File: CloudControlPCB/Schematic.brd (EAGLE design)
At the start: 62.2 x 61.9 mm, 29 parts, among them J1 AUDIO_JACK_TRRSSMD_RA, U1 LPC4088FBD208, U2 SGTL5000XNLA3R2, U3 LD1117S33CTR, X1 PHB_1MM27_2X05_SNT

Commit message: Fixed 1.8V regulator connections
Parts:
- moved U$1 1.27 mm to (15.2, 81.3)
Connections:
- net GND: no longer U$1.4

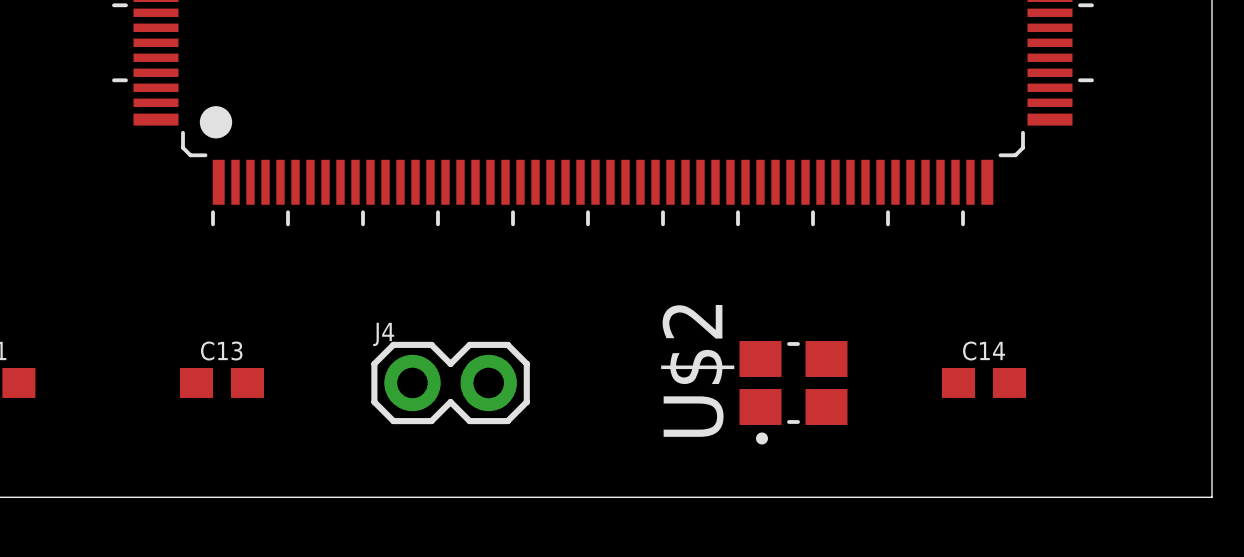
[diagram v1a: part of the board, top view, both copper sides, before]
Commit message: Connected Crystal on layout
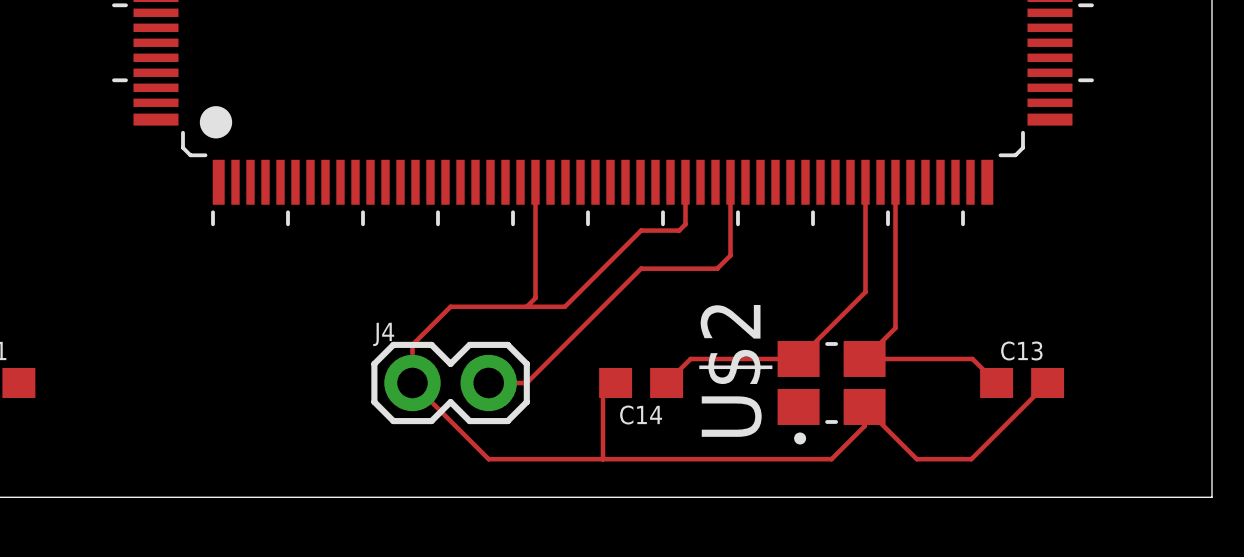
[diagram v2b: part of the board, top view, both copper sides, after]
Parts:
- moved C13 26.7 mm to (63.5, 38.1)
- moved C14 11.4 mm to (50.8, 38.1), turned to 180 degrees
- moved U$2 1.27 mm to (57.1, 38.1)
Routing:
- net GND: track 0.00 -> 45.5 mm
- net N$18: track 0.00 -> 12.3 mm
- net N$3: track 0.00 -> 11.5 mm
- net N$19: track 0.00 -> 11.0 mm
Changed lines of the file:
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@@
 <attribute name="VALUE" x="11.43" y="55.118" size="0.6096" layer="27" font="vector" ratio="20" align="top-center"/>
 </element>
-<element name="C13" library="SparkFun-Capacitors" package="0603" value="18pF" x="36.83" y="38.1">
-<attribute name="NAME" x="36.83" y="38.862" size="0.6096" layer="25" font="vector" ratio="20" align="bottom-center"/>
-<attribute name="PROD_ID" value="CAP-08267" x="113.03" y="-71.12" size="1.778" layer="27" display="off"/>
-<attribute name="VALUE" x="36.83" y="37.338" size="0.6096" layer="27" font="vector" ratio="20" align="top-center"/>
-</element>
-<element name="C14" library="SparkFun-Capacitors" package="0603" value="18pF" x="62.23" y="38.1">
-<attribute name="NAME" x="62.23" y="38.862" size="0.6096" layer="25" font="vector" ratio="20" align="bottom-center"/>
-<attribute name="PROD_ID" value="CAP-08267" x="142.24" y="-71.12" size="1.778" layer="27" display="off"/>
-<attribute name="VALUE" x="62.23" y="37.338" size="0.6096" layer="27" font="vector" ratio="20" align="top-center"/>
+<element name="C13" library="SparkFun-Capacitors" package="0603" value="18pF" x="63.5" y="38.1">
+<attribute name="NAME" x="63.5" y="38.862" size="0.6096" layer="25" font="vector" ratio="20" align="bottom-center"/>
+<attribute name="PROD_ID" value="CAP-08267" x="139.7" y="-71.12" size="1.778" layer="27" display="off"/>
+<attribute name="VALUE" x="63.5" y="37.338" size="0.6096" layer="27" font="vector" ratio="20" align="top-center"/>
+</element>
+<element name="C14" library="SparkFun-Capacitors" package="0603" value="18pF" x="50.8" y="38.1" rot="R180">
+<attribute name="NAME" x="50.8" y="37.338" size="0.6096" layer="25" font="vector" ratio="20" rot="R180" align="bottom-center"/>
+<attribute name="PROD_ID" value="CAP-08267" x="-29.21" y="147.32" size="1.778" layer="27" rot="R180" display="off"/>
+<attribute name="VALUE" x="50.8" y="38.862" size="0.6096" layer="27" font="vector" ratio="20" rot="R180" align="top-center"/>
 </element>
 <element name="C2" library="SparkFun-Capacitors" package="0603" value="0.1uF" x="19.05" y="48.26" rot="R180">
@@
 <attribute name="VALUE" x="27.178" y="69.85" size="0.6096" layer="27" font="vector" ratio="20" rot="R270" align="top-center"/>
 </element>
-<element name="U$2" library="XTAL_FA-238_25.0000MB-C3" package="XTAL_FA-238_25.0000MB-C3" value="XTAL_FA-238_25.0000MB-C3" x="55.88" y="38.1" rot="R90">
-<attribute name="VALUE" x="64.00721875" y="35.7039" size="0.6096" layer="27" rot="R180"/>
+<element name="U$2" library="XTAL_FA-238_25.0000MB-C3" package="XTAL_FA-238_25.0000MB-C3" value="XTAL_FA-238_25.0000MB-C3" x="57.15" y="38.1" rot="R90">
+<attribute name="VALUE" x="60.19721875" y="35.7039" size="0.3048" layer="27" rot="R180"/>
 </element>
 <element name="U1" library="nxp_60_1_1" package="SOT459-1" value="LPC4088FBD208" x="49.53" y="59.69">
@@
 <contactref element="U3" pad="1"/>
 <contactref element="U$1" pad="1"/>
+<wire x1="57.15" y1="35.56" x2="49.53" y2="35.56" width="0.1524" layer="1"/>
+<wire x1="49.53" y1="35.56" x2="45.72" y2="35.56" width="0.1524" layer="1"/>
+<wire x1="45.72" y1="35.56" x2="43.18" y2="38.1" width="0.1524" layer="1"/>
+<wire x1="64.35" y1="38.1" x2="61.81" y2="35.56" width="0.1524" layer="1"/>
+<wire x1="59.99" y1="35.56" x2="58.25" y2="37.3" width="0.1524" layer="1"/>
+<wire x1="61.81" y1="35.56" x2="59.99" y2="35.56" width="0.1524" layer="1"/>
+<wire x1="49.95" y1="38.1" x2="49.53" y2="37.68" width="0.1524" layer="1"/>
+<wire x1="49.53" y1="37.68" x2="49.53" y2="35.56" width="0.1524" layer="1"/>
+<wire x1="57.15" y1="35.56" x2="58.25" y2="36.66" width="0.1524" layer="1"/>
+<wire x1="58.25" y1="36.66" x2="58.25" y2="37.3" width="0.1524" layer="1"/>
+<wire x1="52.28" y1="44.79" x2="52.28" y2="43.39" width="0.1524" layer="1"/>
+<wire x1="52.28" y1="43.39" x2="52.07" y2="43.18" width="0.1524" layer="1"/>
+<wire x1="52.07" y1="43.18" x2="50.8" y2="43.18" width="0.1524" layer="1"/>
+<wire x1="50.8" y1="43.18" x2="48.26" y2="40.64" width="0.1524" layer="1"/>
+<wire x1="48.26" y1="40.64" x2="46.99" y2="40.64" width="0.1524" layer="1"/>
+<wire x1="46.99" y1="40.64" x2="44.45" y2="40.64" width="0.1524" layer="1"/>
+<wire x1="44.45" y1="40.64" x2="43.18" y2="39.37" width="0.1524" layer="1"/>
+<wire x1="43.18" y1="39.37" x2="43.18" y2="38.1" width="0.1524" layer="1"/>
+<wire x1="46.99" y1="40.64" x2="47.28" y2="40.93" width="0.1524" layer="1"/>
+<wire x1="47.28" y1="40.93" x2="47.28" y2="44.79" width="0.1524" layer="1"/>
 <wire x1="60.96" y1="86.78" x2="64.77" y2="88.48" width="0" layer="19" extent="1-1"/>
 <wire x1="60.96" y1="83.13" x2="60.96" y2="86.78" width="0" layer="19" extent="1-1"/>
@@
 <wire x1="11.43" y1="62.23" x2="12.28" y2="55.88" width="0" layer="19" extent="1-1"/>
 <wire x1="18.3388" y1="70.0786" x2="11.43" y2="62.23" width="0" layer="19" extent="1-1"/>
+<wire x1="18.39" y1="78.98" x2="18.3388" y2="70.0786" width="0" layer="19" extent="1-1"/>
 <wire x1="43.87" y1="93.98" x2="53.34" y2="88.9" width="0" layer="19" extent="1-1"/>
 <wire x1="40.08" y1="89.51" x2="43.87" y2="93.98" width="0" layer="19" extent="1-1"/>
-<wire x1="37.68" y1="38.1" x2="34.63" y2="50.94" width="0" layer="19" extent="1-1"/>
-<wire x1="43.18" y1="38.1" x2="37.68" y2="38.1" width="0" layer="19" extent="1-1"/>
-<wire x1="47.28" y1="44.79" x2="43.18" y2="38.1" width="0" layer="19" extent="1-1"/>
-<wire x1="52.28" y1="44.79" x2="47.28" y2="44.79" width="0" layer="19" extent="1-1"/>
-<wire x1="52.78" y1="44.79" x2="52.28" y2="44.79" width="0" layer="19" extent="1-1"/>
-<wire x1="56.98" y1="37.3" x2="52.78" y2="44.79" width="0" layer="19" extent="1-1"/>
-<wire x1="63.08" y1="38.1" x2="56.98" y2="37.3" width="0" layer="19" extent="1-1"/>
-<wire x1="18.39" y1="78.98" x2="11.43" y2="62.23" width="0" layer="19" extent="1-1"/>
-<wire x1="12.7" y1="92.71" x2="18.3388" y2="70.0786" width="0" layer="19" extent="1-1"/>
+<wire x1="52.78" y1="44.79" x2="64.43" y2="51.94" width="0" layer="19" extent="1-1"/>
+<wire x1="52.28" y1="44.79" x2="52.78" y2="44.79" width="0" layer="19" extent="1-1"/>
+<wire x1="12.7" y1="92.71" x2="18.39" y2="78.98" width="0" layer="19" extent="1-1"/>
 </signal>
 <signal name="3.3V">
@@
 <contactref element="U1" pad="35"/>
 <contactref element="J4" pad="2"/>
-<wire x1="45.72" y1="38.1" x2="53.78" y2="44.79" width="0" layer="19" extent="1-1"/>
+<wire x1="45.72" y1="38.1" x2="46.99" y2="38.1" width="0.1524" layer="1"/>
+<wire x1="46.99" y1="38.1" x2="50.8" y2="41.91" width="0.1524" layer="1"/>
+<wire x1="50.8" y1="41.91" x2="53.34" y2="41.91" width="0.1524" layer="1"/>
+<wire x1="53.34" y1="41.91" x2="53.78" y2="42.35" width="0.1524" layer="1"/>
+<wire x1="53.78" y1="42.35" x2="53.78" y2="44.79" width="0.1524" layer="1"/>
 </signal>
 <signal name="N$20">
@@
 <contactref element="C14" pad="1"/>
 <contactref element="U1" pad="44"/>
-<wire x1="54.78" y1="38.9" x2="61.38" y2="38.1" width="0" layer="19" extent="1-1"/>
-<wire x1="58.28" y1="44.79" x2="54.78" y2="38.9" width="0" layer="19" extent="1-1"/>
+<wire x1="58.28" y1="41.13" x2="56.05" y2="38.9" width="0.1524" layer="1"/>
+<wire x1="58.28" y1="41.13" x2="58.28" y2="44.79" width="0.1524" layer="1"/>
+<wire x1="56.05" y1="38.9" x2="52.45" y2="38.9" width="0.1524" layer="1"/>
+<wire x1="52.45" y1="38.9" x2="51.65" y2="38.1" width="0.1524" layer="1"/>
 </signal>
 <signal name="N$19">
@@
 <contactref element="C13" pad="1"/>
 <contactref element="U1" pad="46"/>
-<wire x1="56.98" y1="38.9" x2="59.28" y2="44.79" width="0" layer="19" extent="1-1"/>
-<wire x1="35.98" y1="38.1" x2="56.98" y2="38.9" width="0" layer="19" extent="1-1"/>
+<wire x1="59.28" y1="39.93" x2="58.25" y2="38.9" width="0.1524" layer="1"/>
+<wire x1="59.28" y1="39.93" x2="59.28" y2="44.79" width="0.1524" layer="1"/>
+<wire x1="61.85" y1="38.9" x2="58.25" y2="38.9" width="0.1524" layer="1"/>
+<wire x1="61.85" y1="38.9" x2="62.65" y2="38.1" width="0.1524" layer="1"/>
 </signal>
 </signals>

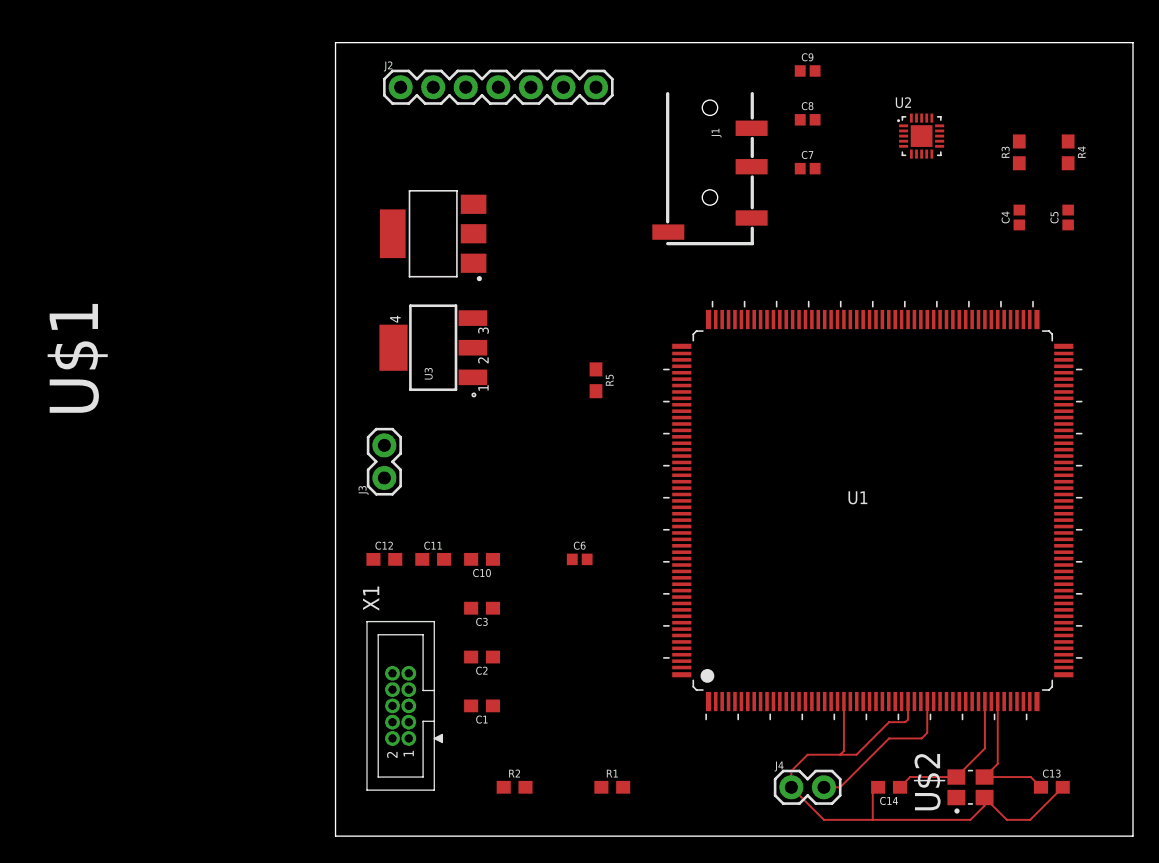
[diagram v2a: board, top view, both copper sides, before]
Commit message: added more routes
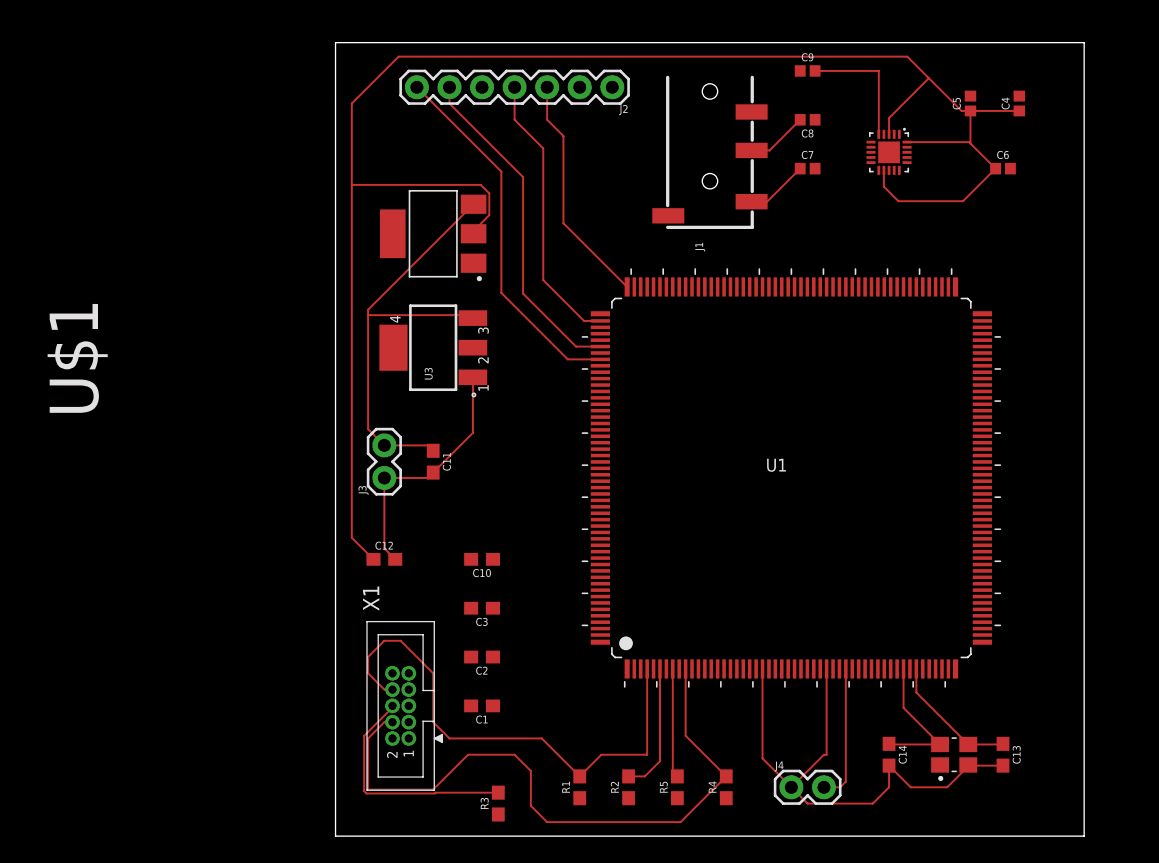
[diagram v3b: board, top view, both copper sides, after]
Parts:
- moved R3 65.1 mm to (20.3, 36.8)
- moved R4 56.3 mm to (38.1, 38.1), turned to 90 degrees
- moved C6 44.9 mm to (59.7, 86.4)
- moved R5 32.4 mm to (34.3, 38.1), turned to 90 degrees
- moved J2 16.5 mm to (29.2, 92.7), turned to 180 degrees
- moved C5 11.7 mm to (57.1, 91.4)
- moved C4 8.89 mm to (61.0, 91.4)
- moved R2 8.89 mm to (30.5, 38.1), turned to 90 degrees
- moved C11 7.62 mm to (15.2, 63.5), turned to 270 degrees
- moved U1 6.84 mm to (43.2, 62.2)
- moved C13 4.58 mm to (59.7, 40.6), turned to 270 degrees
- moved U2 2.84 mm to (50.8, 87.6), turned to 270 degrees
- moved U$2 2.84 mm to (55.9, 40.6)
- moved C14 2.54 mm to (50.8, 40.6), turned to 270 degrees
- moved R1 2.54 mm to (26.7, 38.1), turned to 90 degrees
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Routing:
- net N$20: track 0.00 -> 133.9 mm
- net N$14: track 0.00 -> 50.4 mm
- net N$12: track 0.00 -> 40.0 mm
- net VCC: track 0.00 -> 35.0 mm
- net SS: track 0.00 -> 28.6 mm
- net CLK: track 0.00 -> 26.2 mm
- net MOSI: track 0.00 -> 21.7 mm
- net NRFCSN: track 0.00 -> 18.2 mm
- net N$9: track 0.00 -> 18.1 mm
- net GND: track 45.5 -> 60.8 mm
- net N$13: track 0.00 -> 10.1 mm
- net N$15: track 0.00 -> 9.92 mm
- net N$16: track 0.00 -> 8.53 mm
- net TIP: track 0.00 -> 4.86 mm
- net RING1: track 0.00 -> 4.78 mm
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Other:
- board size 62.2 x 61.9 mm -> 58.4 x 61.9 mm

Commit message: More routing on layout
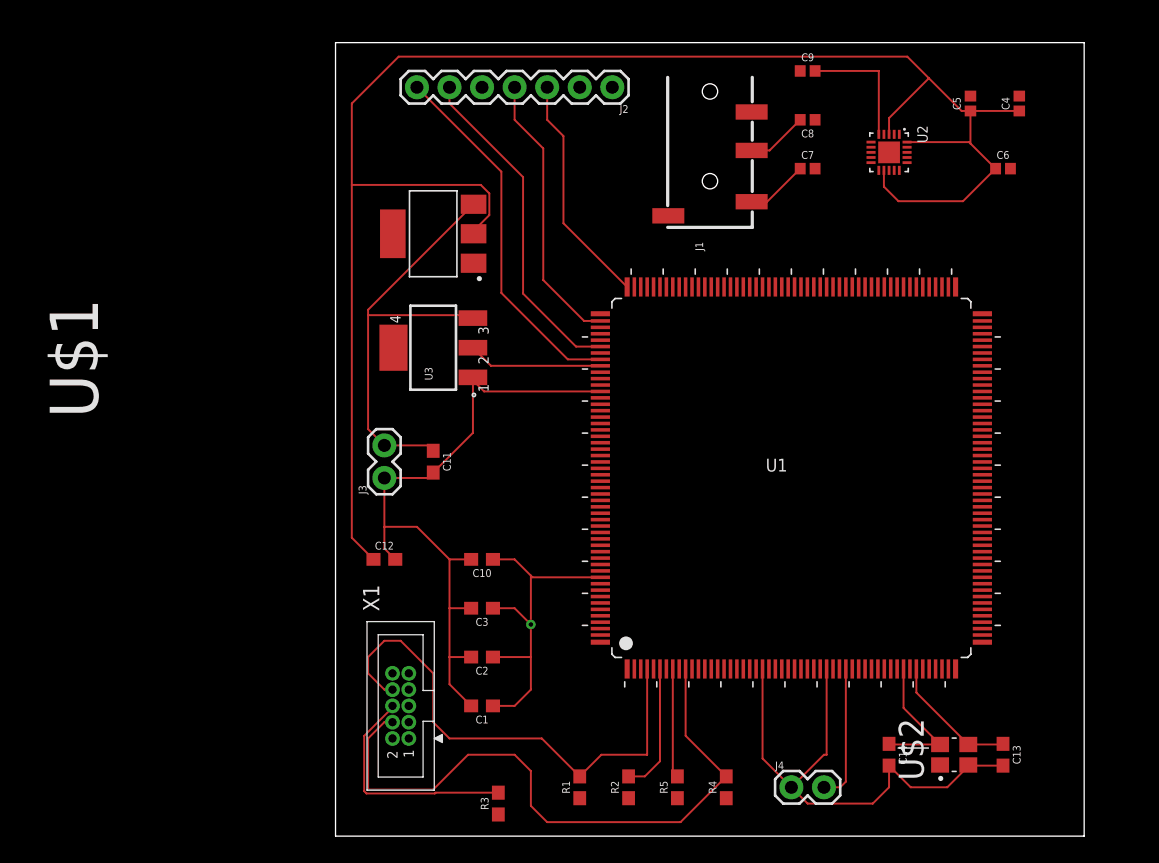
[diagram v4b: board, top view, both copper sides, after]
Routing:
- net 3.3V: track 0.00 -> 38.3 mm, vias 0 -> 1
- net GND: track 60.8 -> 94.4 mm

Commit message: finished routing
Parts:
- added C15: 0.1uF, SparkFun-Capacitors:0603
- moved C3 38.6 mm to (27.9, 89.7), turned to 0 degrees
- moved C2 23.3 mm to (41.9, 43.7), turned to 270 degrees
- moved C1 20.1 mm to (39.1, 43.7), turned to 270 degrees
- moved C12 18.1 mm to (22.6, 70.1), turned to 270 degrees
- moved U3 11.6 mm to (17.0, 61.0)
- moved C6 11.2 mm to (48.8, 84.1), turned to 270 degrees
- moved U$1 10.0 mm to (16.8, 71.4)
- moved J3 7.96 mm to (13.7, 54.6), turned to 180 degrees
- moved C5 6.36 mm to (50.8, 91.2)
- moved C13 5.95 mm to (55.1, 44.5), turned to 0 degrees
- moved C4 5.95 mm to (55.4, 89.4)
- moved C9 5.58 mm to (49.3, 91.2), turned to 270 degrees
- moved C10 5.39 mm to (22.9, 59.7), turned to 270 degrees
- moved C11 4.66 mm to (19.3, 65.8), turned to 180 degrees
- moved C14 3.82 mm to (50.5, 44.5), turned to 180 degrees
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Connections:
- net GND: now also C15.2
- net VCC: now also C15.1
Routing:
- net N$17: track 0.00 -> 80.1 mm, vias 0 -> 1
- net N$20: track 133.9 -> 78.5 mm, vias 0 -> 3
- net N$4: track 0.00 -> 50.6 mm, vias 0 -> 2
- net N$8: track 0.00 -> 44.2 mm, vias 0 -> 2
- net N$9: track 18.1 -> 51.6 mm
- net N$11: track 0.00 -> 33.3 mm, vias 0 -> 2
- net N$16: track 8.53 -> 37.8 mm, vias 0 -> 1
- net GND: track 94.4 -> 67.7 mm, vias 0 -> 26
- net N$6: track 0.00 -> 23.1 mm
- net N$7: track 0.00 -> 22.6 mm, vias 0 -> 2
- net N$13: track 10.1 -> 29.8 mm, vias 0 -> 1
- net N$5: track 0.00 -> 17.3 mm
- net VCC: track 35.0 -> 46.6 mm
- net N$10: track 0.00 -> 10.3 mm
- net 3.3V: track 38.3 -> 47.3 mm, vias 1 -> 16
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- added copper zone on layer 15, net 3.3V
- added copper zone on layer 2, net GND
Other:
- board size 58.4 x 61.9 mm -> 57.1 x 61.9 mm
- board text added: "CLOUD CONTROL"
- board text added: "Reed Taylor Andrew Thompson Brent Morada Anna Lee Jair Santiago Carranza"
